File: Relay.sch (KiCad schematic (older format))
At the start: 0 parts

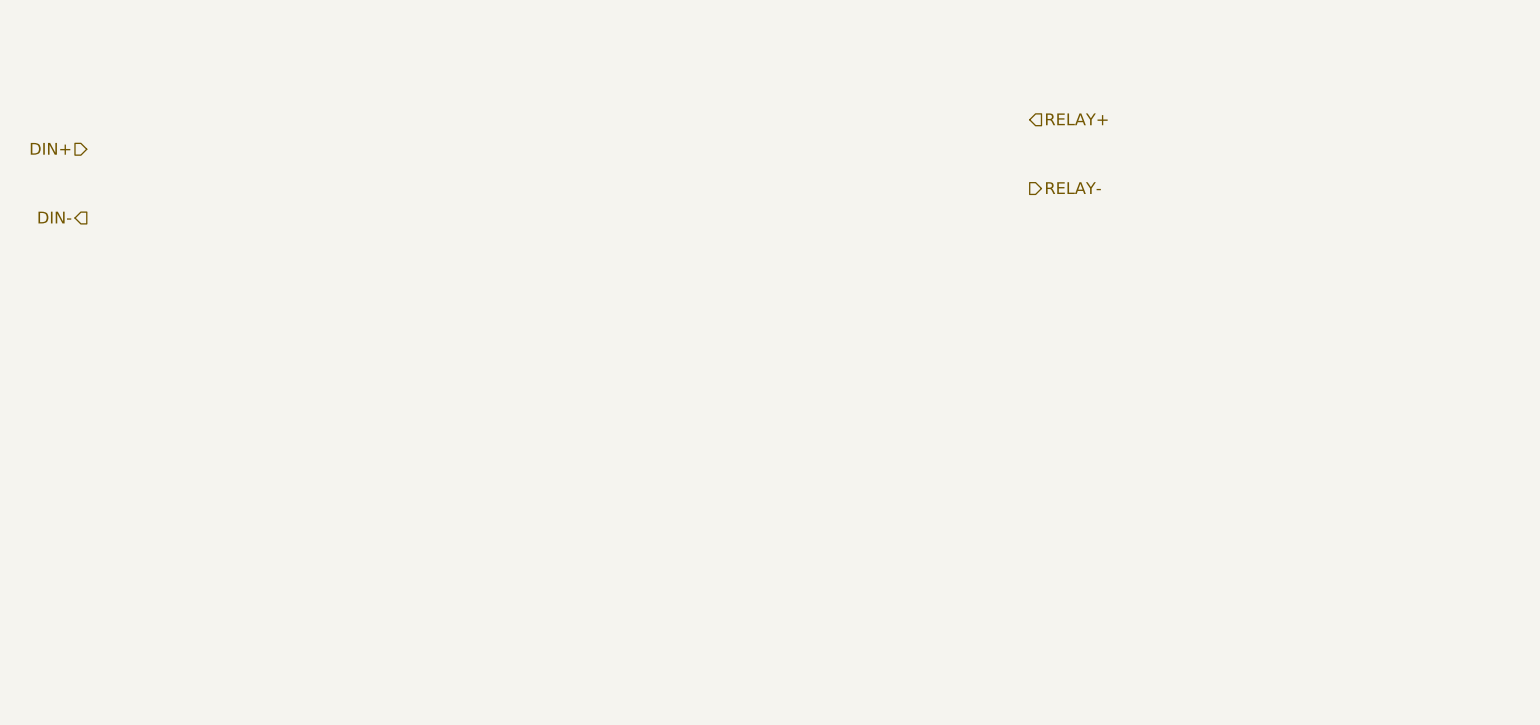
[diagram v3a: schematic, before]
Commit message: Created first schematic for Relay module
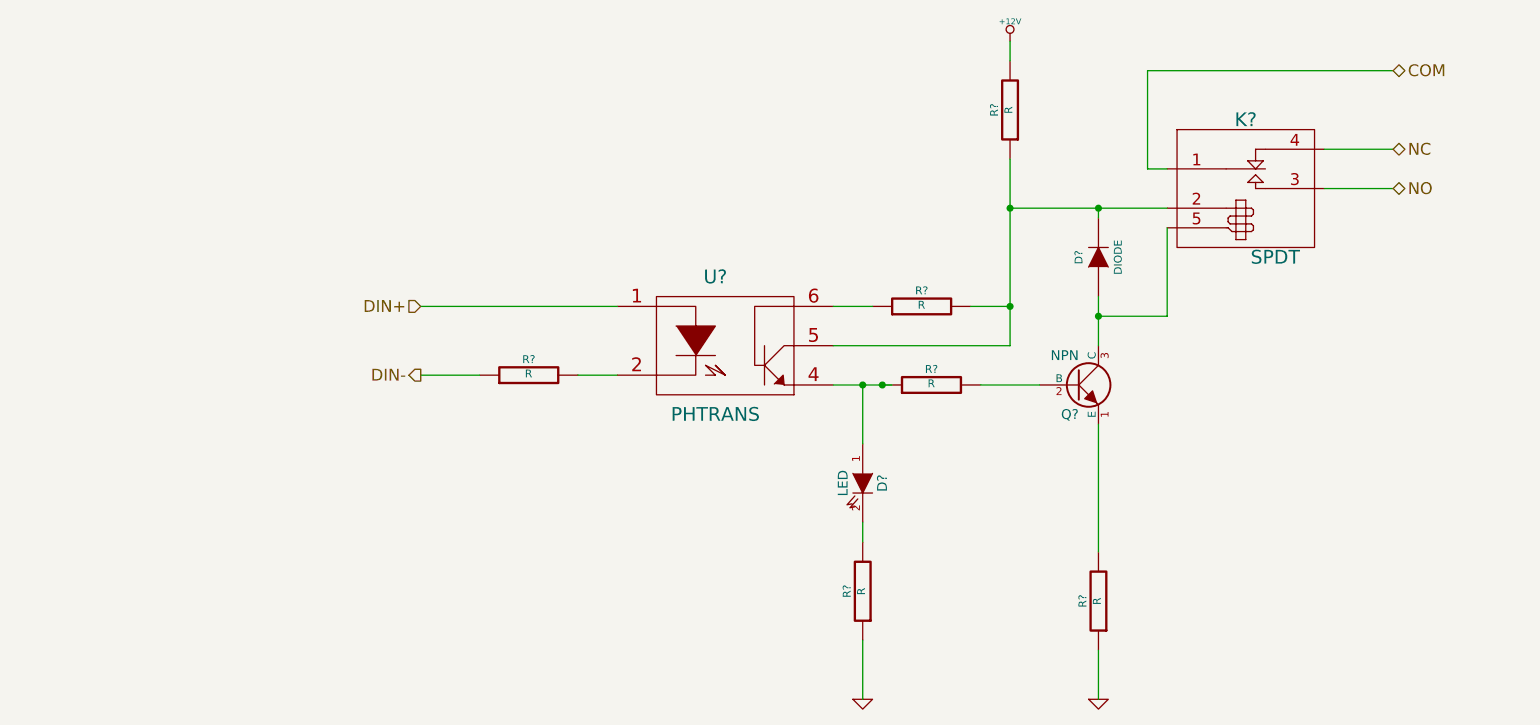
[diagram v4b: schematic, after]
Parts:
- added D?: LED, ~, symbol LED
- added D?: DIODE, ~, symbol DIODE
- added K?: SPDT, ~, symbol SPDT
- added Q?: NPN, ~, symbol NPN
- added R? (x6): R, ~, symbol R
- added U?: PHTRANS, ~, symbol PHTRANS
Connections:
- net labels added: +12V, COM, GND, NC, NO
- net labels removed: RELAY+, RELAY-
- wire segments 0 -> 25
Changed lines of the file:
@@
 LIBS:contrib
 LIBS:valves
+LIBS:BenchBudEE
 LIBS:BenchBudEE-cache
 EELAYER 27 0
@@
 Sheet 4 8
 Title ""
-Date "8 feb 2014"
+Date "9 feb 2014"
 Rev ""
 Comp ""
@@
 Comment4 ""
 $EndDescr
-Text HLabel 2700 2600 0    60   Input ~ 0
+Text HLabel 4400 3400 0    60   Input ~ 0
 DIN+
-Text HLabel 2700 2950 0    60   Output ~ 0
+Text HLabel 4400 3750 0    60   Output ~ 0
 DIN-
-Text HLabel 7500 2450 2    60   Input ~ 0
-RELAY+
-Text HLabel 7500 2800 2    60   Output ~ 0
-RELAY-
+Text HLabel 9350 2600 2    60   BiDi ~ 0
+NC
+Text HLabel 9350 2800 2    60   BiDi ~ 0
+NO
+$Comp
+L PHTRANS U?
+U 1 1 52F74091
+P 5950 3600
+F 0 "U?" H 5900 3950 70  0000 C CNN
+F 1 "PHTRANS" H 5900 3250 70  0000 C CNN
+F 2 "~" H 5950 3600 60  0000 C CNN
+F 3 "~" H 5950 3600 60  0000 C CNN
+	1    5950 3600
+	1    0    0    -1
+$EndComp
+$Comp
+L R R?
+U 1 1 52F740A0
+P 7000 3800
+F 0 "R?" V 7080 3800 40  0000 C CNN
+F 1 "R" V 7007 3801 40  0000 C CNN
+F 2 "~" V 6930 3800 30  0000 C CNN
+F 3 "~" H 7000 3800 30  0000 C CNN
+	1    7000 3800
+	0    -1   -1   0
+$EndComp
+$Comp
+L NPN Q?
+U 1 1 52F740AF
+P 7750 3800
+F 0 "Q?" H 7750 3650 50  0000 R CNN
+F 1 "NPN" H 7750 3950 50  0000 R CNN
+F 2 "~" H 7750 3800 60  0000 C CNN
+F 3 "~" H 7750 3800 60  0000 C CNN
+	1    7750 3800
+	1    0    0    -1
+$EndComp
+$Comp
+L LED D?
+U 1 1 52F740BE
+P 6650 4300
+F 0 "D?" H 6650 4400 50  0000 C CNN
+F 1 "LED" H 6650 4200 50  0000 C CNN
+F 2 "~" H 6650 4300 60  0000 C CNN
+F 3 "~" H 6650 4300 60  0000 C CNN
+	1    6650 4300
+	0    1    1    0
+$EndComp
+$Comp
+L SPDT K?
+U 1 1 52F7444C
+P 8600 2650
+F 0 "K?" H 8600 2850 70  0000 C CNN
+F 1 "SPDT" H 8750 2150 70  0000 C CNN
+F 2 "~" H 8600 2650 60  0000 C CNN
+F 3 "~" H 8600 2650 60  0000 C CNN
+	1    8600 2650
+	1    0    0    -1
+$EndComp
+Text HLabel 9350 2200 2    60   BiDi ~ 0
+COM
+Wire Wire Line
+	9000 2600 9350 2600
+Wire Wire Line
+	9350 2800 9000 2800
+Wire Wire Line
+	9350 2200 8100 2200
+Wire Wire Line
+	8100 2200 8100 2700
+Wire Wire Line
+	8100 2700 8200 2700
+Wire Wire Line
+	6500 3800 6800 3800
+Connection ~ 6750 3800
+Wire Wire Line
+	7250 3800 7550 3800
+Wire Wire Line
+	7850 3350 7850 3600
+Wire Wire Line
+	7850 3450 8200 3450
+Wire Wire Line
+	7850 4000 7850 4650
+$Comp
+L R R?
+U 1 1 52F744D2
+P 7850 4900
+F 0 "R?" V 7930 4900 40  0000 C CNN
+F 1 "R" V 7857 4901 40  0000 C CNN
+F 2 "~" V 7780 4900 30  0000 C CNN
+F 3 "~" H 7850 4900 30  0000 C CNN
+	1    7850 4900
+	-1   0    0    1
+$EndComp
+$Comp
+L GND #PWR?
+U 1 1 52F744DA
+P 7850 5400
+F 0 "#PWR?" H 7850 5400 30  0001 C CNN
+F 1 "GND" H 7850 5330 30  0001 C CNN
+F 2 "" H 7850 5400 60  0000 C CNN
+F 3 "" H 7850 5400 60  0000 C CNN
+	1    7850 5400
+	1    0    0    -1
+$EndComp
+Wire Wire Line
+	7850 5400 7850 5150
+$Comp
+L R R?
+U 1 1 52F744FD
+P 6650 4850
+F 0 "R?" V 6730 4850 40  0000 C CNN
+F 1 "R" V 6657 4851 40  0000 C CNN
+F 2 "~" V 6580 4850 30  0000 C CNN
+F 3 "~" H 6650 4850 30  0000 C CNN
+	1    6650 4850
+	-1   0    0    1
+$EndComp
+Wire Wire Line
+	6650 4100 6650 3800
+Connection ~ 6650 3800
+Wire Wire Line
+	6650 4500 6650 4600
+$Comp
+L GND #PWR?
+U 1 1 52F7451F
+P 6650 5400
+F 0 "#PWR?" H 6650 5400 30  0001 C CNN
+F 1 "GND" H 6650 5330 30  0001 C CNN
+F 2 "" H 6650 5400 60  0000 C CNN
+F 3 "" H 6650 5400 60  0000 C CNN
+	1    6650 5400
+	1    0    0    -1
+$EndComp
+Wire Wire Line
+	6650 5400 6650 5100
+$Comp
+L +12V #PWR?
+U 1 1 52F74537
+P 7400 2050
+F 0 "#PWR?" H 7400 2000 20  0001 C CNN
+F 1 "+12V" H 7400 2150 30  0000 C CNN
+F 2 "" H 7400 2050 60  0000 C CNN
+F 3 "" H 7400 2050 60  0000 C CNN
+	1    7400 2050
+	1    0    0    -1
+$EndComp
+$Comp
+L R R?
+U 1 1 52F74544
+P 7400 2400
+F 0 "R?" V 7480 2400 40  0000 C CNN
+F 1 "R" V 7407 2401 40  0000 C CNN
+F 2 "~" V 7330 2400 30  0000 C CNN
+F 3 "~" H 7400 2400 30  0000 C CNN
+	1    7400 2400
+	-1   0    0    1
+$EndComp
+Wire Wire Line
+	7400 2050 7400 2150
+Wire Wire Line
+	7400 2650 7400 3600
+Wire Wire Line
+	7400 2900 8200 2900
+Wire Wire Line
+	7400 3600 6500 3600
+Connection ~ 7400 2900
+$Comp
+L R R?
+U 1 1 52F74581
+P 6950 3400
+F 0 "R?" V 7030 3400 40  0000 C CNN
+F 1 "R" V 6957 3401 40  0000 C CNN
+F 2 "~" V 6880 3400 30  0000 C CNN
+F 3 "~" H 6950 3400 30  0000 C CNN
+	1    6950 3400
+	0    -1   -1   0
+$EndComp
+Wire Wire Line
+	6700 3400 6500 3400
+Wire Wire Line
+	7200 3400 7400 3400
+Connection ~ 7400 3400
+$Comp
+L R R?
+U 1 1 52F745B4
+P 4950 3750
+F 0 "R?" V 5030 3750 40  0000 C CNN
+F 1 "R" V 4957 3751 40  0000 C CNN
+F 2 "~" V 4880 3750 30  0000 C CNN
+F 3 "~" H 4950 3750 30  0000 C CNN
+	1    4950 3750
+	0    -1   -1   0
+$EndComp
+Wire Wire Line
+	5400 3750 5200 3750
+Wire Wire Line
+	5400 3400 4400 3400
+Wire Wire Line
+	4700 3750 4400 3750
+Wire Wire Line
+	8200 3450 8200 3000
+$Comp
+L DIODE D?
+U 1 1 52F7462E
+P 7850 3150
+F 0 "D?" H 7850 3250 40  0000 C CNN
+F 1 "DIODE" H 7850 3050 40  0000 C CNN
+F 2 "~" H 7850 3150 60  0000 C CNN
+F 3 "~" H 7850 3150 60  0000 C CNN
+	1    7850 3150
+	0    -1   -1   0
+$EndComp
+Wire Wire Line
+	7850 2950 7850 2900
+Connection ~ 7850 2900
+Connection ~ 7850 3450
 $EndSCHEMATC

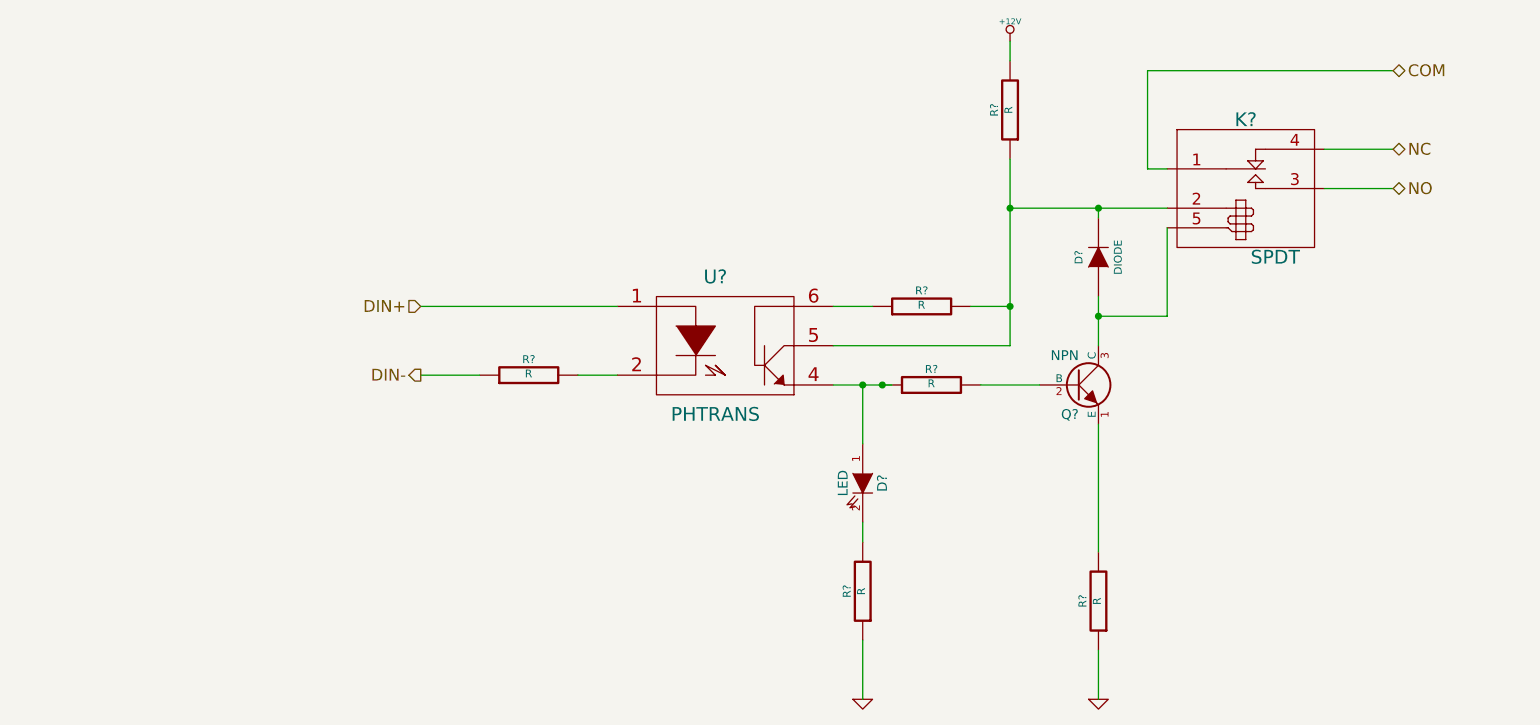
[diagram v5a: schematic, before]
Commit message: Created the Arduino module and then connected all the modules in the main schematic
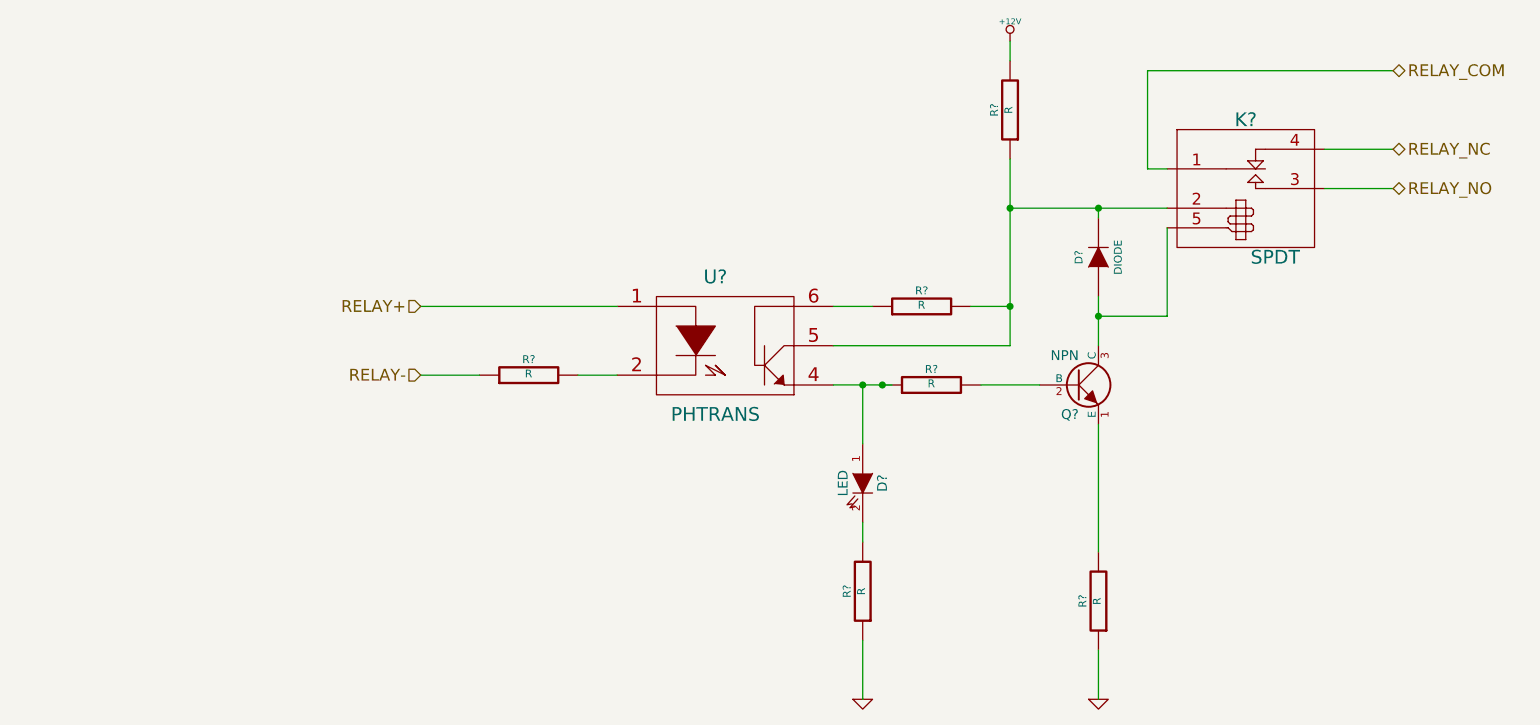
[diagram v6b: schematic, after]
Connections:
- net labels added: RELAY+, RELAY-, RELAY_COM, RELAY_NC, RELAY_NO
- net labels removed: COM, DIN+, DIN-, NC, NO
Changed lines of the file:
@@
 $Descr A4 11693 8268
 encoding utf-8
-Sheet 4 9
+Sheet 7 9
 Title ""
 Date "10 feb 2014"
@@
 $EndDescr
 Text HLabel 4400 3400 0    60   Input ~ 0
-DIN+
-Text HLabel 4400 3750 0    60   Output ~ 0
-DIN-
+RELAY+
+Text HLabel 4400 3750 0    60   Input ~ 0
+RELAY-
 Text HLabel 9350 2600 2    60   BiDi ~ 0
-NC
+RELAY_NC
 Text HLabel 9350 2800 2    60   BiDi ~ 0
-NO
+RELAY_NO
 $Comp
 L PHTRANS U?
@@
 $EndComp
 Text HLabel 9350 2200 2    60   BiDi ~ 0
-COM
+RELAY_COM
 Wire Wire Line
 	9000 2600 9350 2600
